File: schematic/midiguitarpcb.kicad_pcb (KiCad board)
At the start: 2 copper layers, 50 x 50 mm, 35 parts, among them J1 USB_C_Receptacle_USB2.0_16P, J2 AudioJack3_Switch, SW1 SW_Omron_B3FS, U1 AMS1117-3.3, U2 DIN-504D-M5, U3 STM32H743ZITx

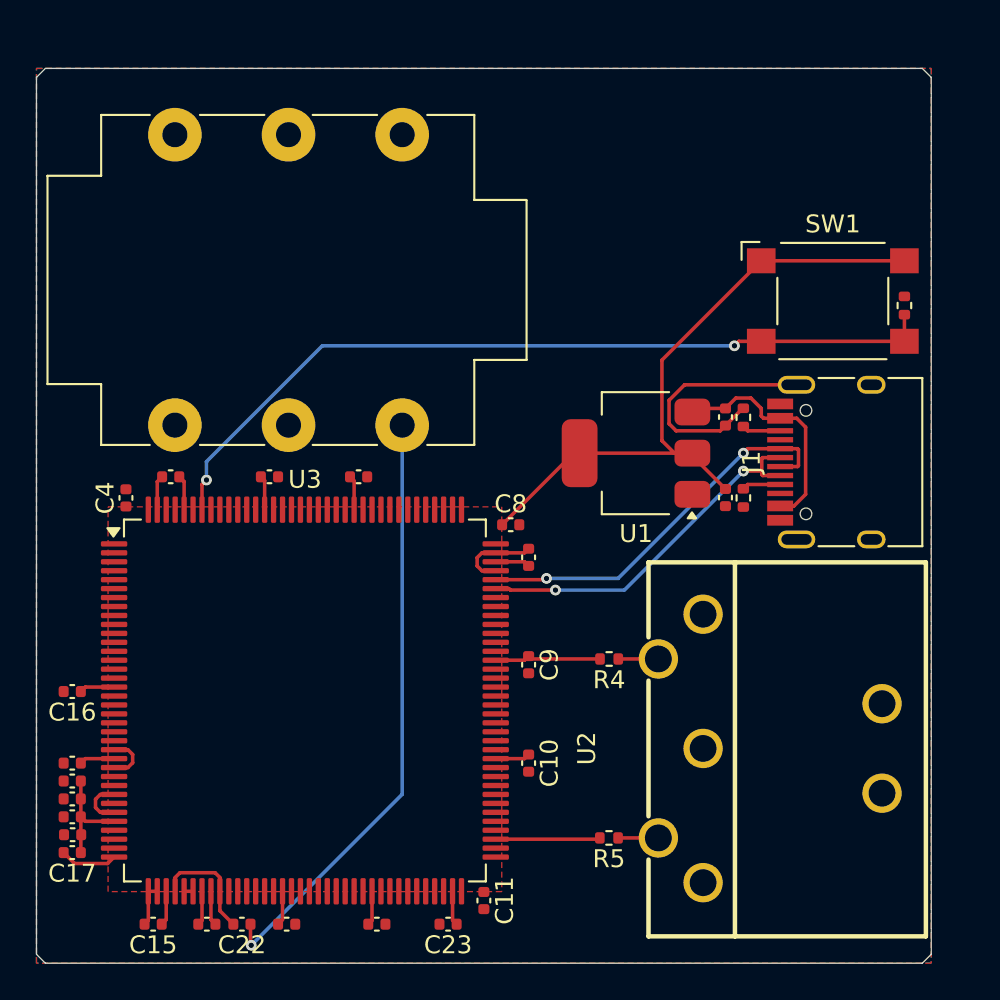
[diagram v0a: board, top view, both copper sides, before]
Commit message: chore(wip): about to remove usb code
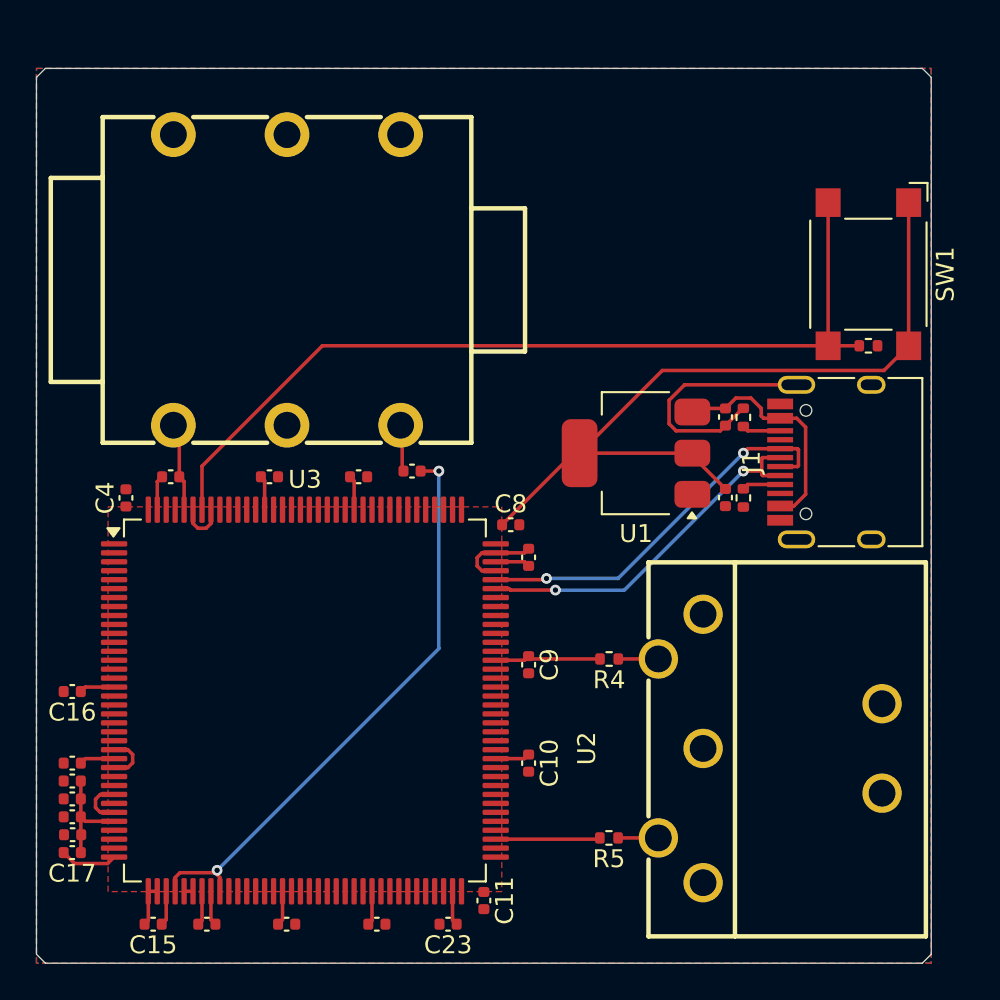
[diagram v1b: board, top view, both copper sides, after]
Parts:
- removed J2: AudioJack3_Switch, Connector_Audio:Jack_6.35mm_Neutrik_NMJ6HCD2_Horizontal
- added CN1: NMJ6HCD2, audio:AUDIO-TH_NMJ6HCD2, F.Cu at (64.0, 61.8)
- moved C22 27.0 mm to (71.0, 72.5)
- moved R1 3.02 mm to (96.5, 65.5), turned to 0 degrees
- moved SW1 2.49 mm to (96.5, 61.5), turned to -90 degrees
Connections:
- C22 pad 1: Net-(C22-Pad1) -> Net-(U3-PA4)
- C22 pad 2: Net-(U3-PA4) -> Net-(CN1-T)
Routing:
- net Net-(C22-Pad1): track 33.8 -> 0.00 mm, vias 1 -> 0
- net Net-(U3-PA4): track 6.41 -> 32.7 mm, vias 0 -> 2
- net +3V3: track 64.8 -> 71.4 mm
- net GND: track 31.9 -> 37.7 mm
- net Net-(U3-BOOT0): track 46.1 -> 49.9 mm, vias 2 -> 0
- net Net-(CN1-T): track 0.00 -> 2.59 mm

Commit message: fix(pcb): midi resistors swapped
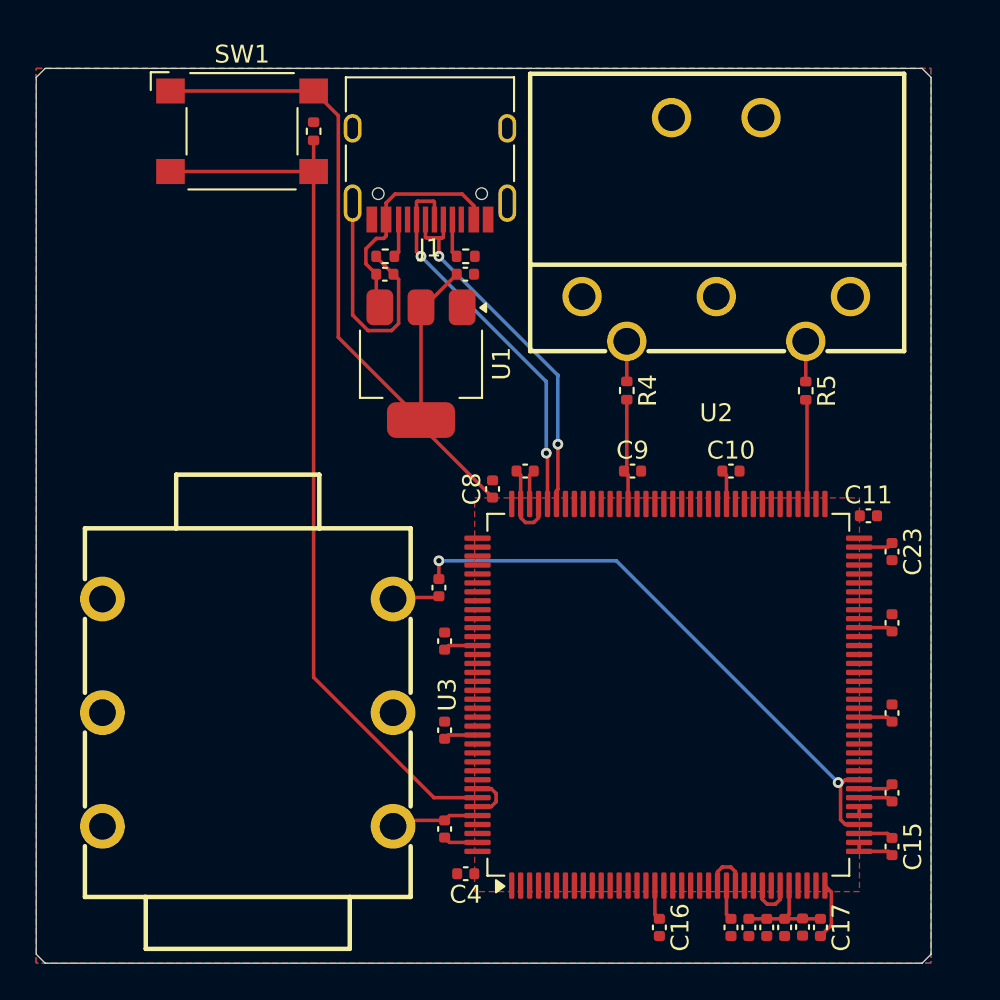
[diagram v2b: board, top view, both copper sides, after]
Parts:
- R4: value 10 -> 33
- R5: value 33 -> 10
- moved C17 42.0 mm to (93.8, 98.0), turned to -90 degrees
- moved C15 41.5 mm to (97.8, 93.5), turned to -90 degrees
- moved C1 41.1 mm to (92.8, 98.0), turned to -90 degrees
- moved C2 40.3 mm to (91.8, 98.0), turned to -90 degrees
- moved C3 39.5 mm to (90.8, 98.0), turned to -90 degrees
- moved C21 39.0 mm to (97.8, 90.5), turned to 90 degrees
- moved C18 38.7 mm to (89.8, 98.0), turned to -90 degrees
- moved C20 37.9 mm to (88.8, 98.0), turned to -90 degrees
- moved SW1 35.9 mm to (61.5, 53.5), turned to 0 degrees
- moved C14 35.8 mm to (97.8, 86.0), turned to 90 degrees
- moved C16 35.4 mm to (84.8, 98.0), turned to -90 degrees
- moved C12 33.4 mm to (97.8, 81.0), turned to 90 degrees
- moved R1 33.2 mm to (65.5, 53.5), turned to 90 degrees
- moved C23 32.4 mm to (97.8, 77.0), turned to -90 degrees
- moved C11 30.4 mm to (96.5, 75.0), turned to 0 degrees
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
